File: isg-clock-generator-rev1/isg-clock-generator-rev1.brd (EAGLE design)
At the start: 76.2 x 76.2 mm, 160 parts, among them IC1 LMK03318RHSR, IC4 TPS7A8001DRBR, IC5 TPS7A8001DRBR, Q1 7M50072001, X1 OUT2_P, X2 OUT2_N, X3 OUT0_P, X4 PRIREF_P, X5 PRIREF_N, X6 V_IN_EXT

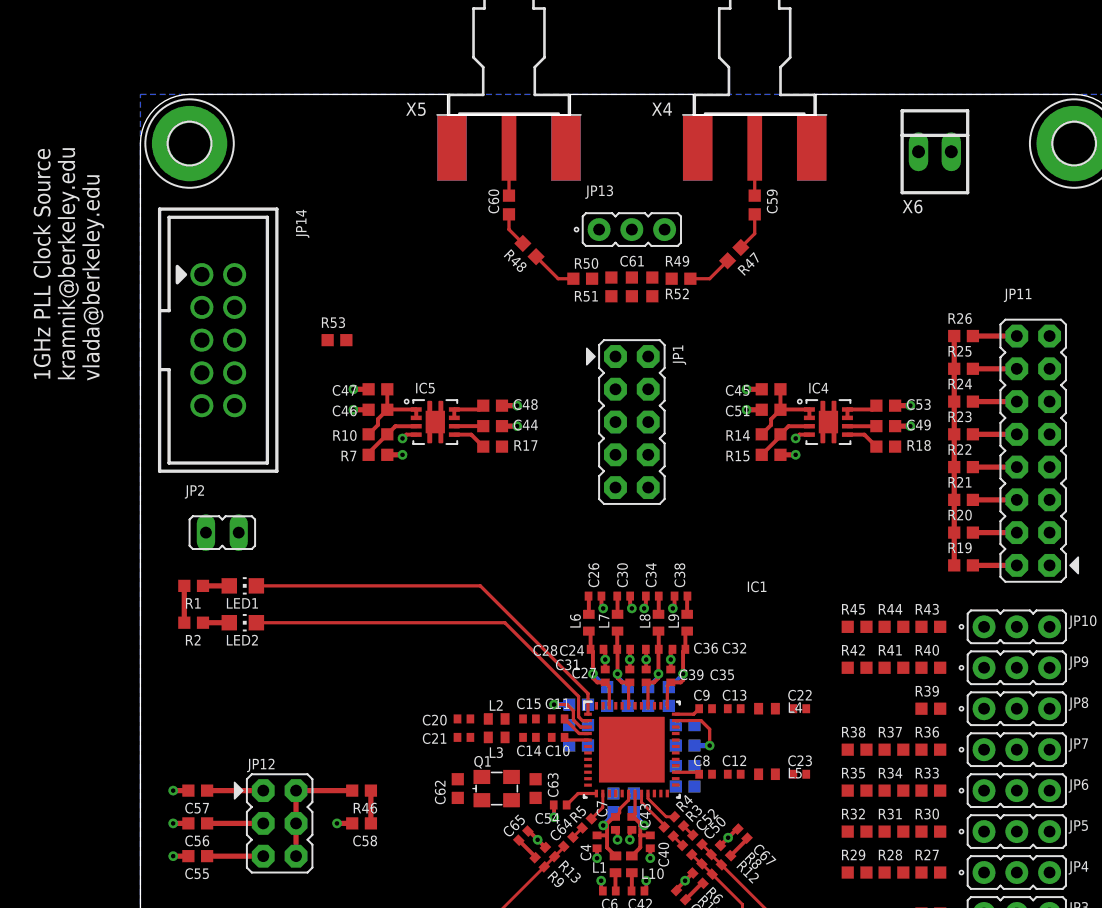
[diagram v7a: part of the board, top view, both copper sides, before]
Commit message: Crystal package fixed and routed
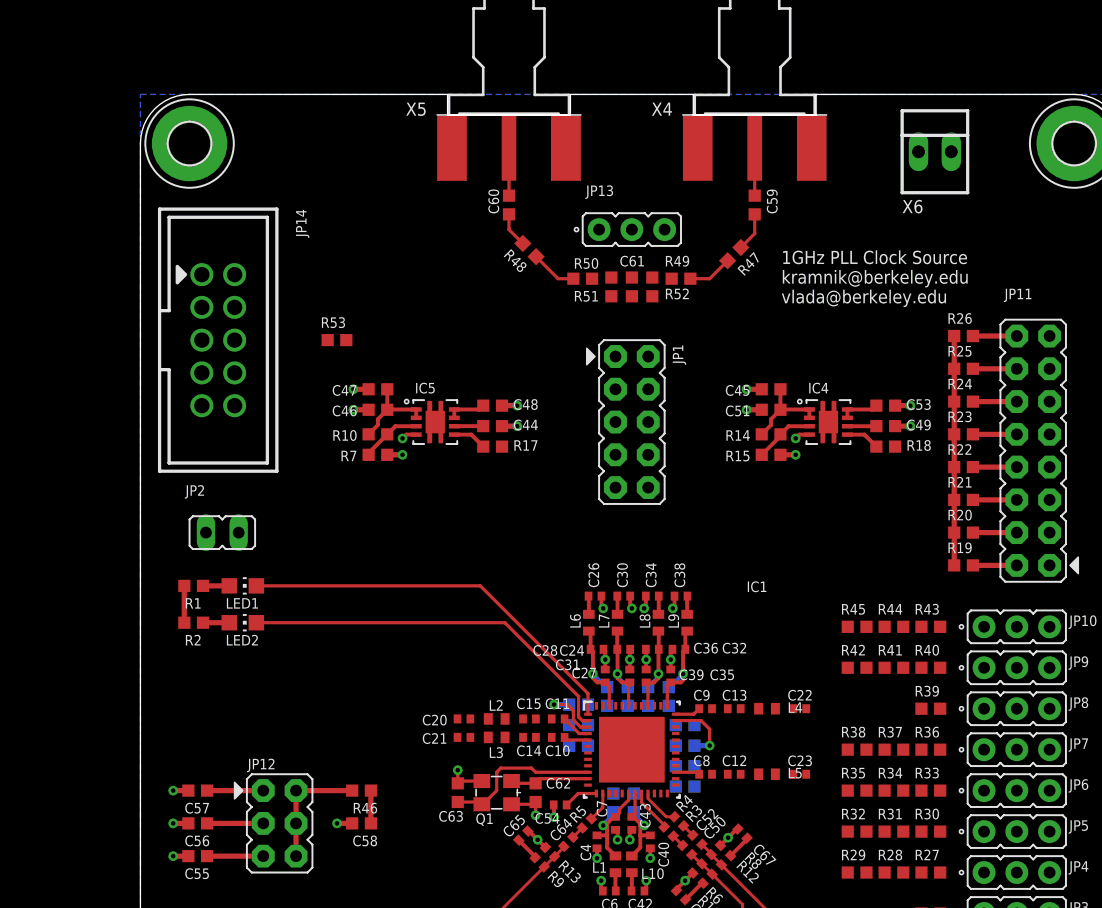
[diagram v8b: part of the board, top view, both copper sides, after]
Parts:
- Q1: device crystal-geyer_V1_0:3.2X2.5_KX-7 -> isg-clock-generator:3.2X2.5_KX-7
- moved C62 6.04 mm to (30.6, 22.1), turned to 270 degrees
- moved C63 6.04 mm to (24.6, 22.1), turned to 90 degrees
- moved Q1 0.32 mm to (27.6, 22.1), turned to 180 degrees
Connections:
- net GND: now also Q1.2, Q1.4
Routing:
- net SECREF_P: track 0.00 -> 12.3 mm
- net SECREF_N: track 0.00 -> 6.15 mm
- net GND: track 41.3 -> 47.2 mm, vias 44 -> 46
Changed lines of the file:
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@@
 <wire x1="23.8125" y1="76.2" x2="3.81" y2="76.2" width="0" layer="20"/>
 <wire x1="3.81" y1="76.2" x2="0" y2="72.39" width="0" layer="20" curve="90"/>
-<text x="-3.175" y="53.975" size="1.27" layer="21" rot="R90">1GHz PLL Clock Source
+<text x="49.68875" y="60.0075" size="1.016" layer="21">1GHz PLL Clock Source
 kramnik@berkeley.edu
 vlada@berkeley.edu</text>
@@
 <attribute name="VALUE" x="27.6225" y="1.905" size="1.016" layer="27" font="vector" ratio="16" rot="R90"/>
 </element>
-<element name="Q1" library="crystal-geyer_V1_0" library_urn="urn:adsk.eagle:library:203" package="3.2X2.5_KX-7" package3d_urn="urn:adsk.eagle:package:11924/1" value="7M50072001" x="27.6225" y="22.38375" smashed="yes">
-<attribute name="NAME" x="25.8225" y="24.08375" size="0.8128" layer="25" font="vector" ratio="16"/>
+<element name="Q1" library="isg-clock-generator" package="3.2X2.5_KX-7" package3d_urn="urn:adsk.eagle:package:11924/1" value="7M50072001" x="27.6225" y="22.06625" smashed="yes" rot="R180">
+<attribute name="NAME" x="25.98125" y="19.63875" size="0.8128" layer="25" font="vector" ratio="16"/>
 </element>
 <element name="C1" library="rcl-modified-footprints" package="C0603" package3d_urn="urn:adsk.eagle:package:23616/2" value="CAP CER 10uF 6.3V X5R 0603" x="33.9725" y="28.8925" smashed="yes" rot="MR180">
@@
 <attribute name="VALUE" x="34.544" y="67.437" size="0.8128" layer="27" font="vector" ratio="16"/>
 </element>
-<element name="C62" library="rcl-modified-footprints" package="C0603" package3d_urn="urn:adsk.eagle:package:23616/2" value="DNP" x="24.60625" y="22.38375" smashed="yes" rot="R90">
-<attribute name="NAME" x="23.65375" y="21.11375" size="0.8128" layer="25" font="vector" ratio="16" rot="R90"/>
-</element>
-<element name="C63" library="rcl-modified-footprints" package="C0603" package3d_urn="urn:adsk.eagle:package:23616/2" value="DNP" x="30.63875" y="22.38375" smashed="yes" rot="R270">
-<attribute name="NAME" x="31.59125" y="23.65375" size="0.8128" layer="25" font="vector" ratio="16" rot="R270"/>
+<element name="C62" library="rcl-modified-footprints" package="C0603" package3d_urn="urn:adsk.eagle:package:23616/2" value="DNP" x="30.63875" y="22.06625" smashed="yes" rot="R270">
+<attribute name="NAME" x="31.4325" y="22.38375" size="0.8128" layer="25" font="vector" ratio="16"/>
+</element>
+<element name="C63" library="rcl-modified-footprints" package="C0603" package3d_urn="urn:adsk.eagle:package:23616/2" value="DNP" x="24.60625" y="22.06625" smashed="yes" rot="R90">
+<attribute name="NAME" x="25.0825" y="20.6375" size="0.8128" layer="25" font="vector" ratio="16" rot="R180"/>
 </element>
 <element name="JP14" library="Kramnik's Library" package="CON_OST_302-S101" value="CON_OST_302-S101" x="6.0325" y="57.15" smashed="yes" rot="R270">
@@
 <wire x1="35.7425" y1="37.30625" x2="35.7425" y2="36.48875" width="0.3048" layer="1"/>
 <wire x1="35.7425" y1="36.48875" x2="35.8775" y2="36.35375" width="0.3048" layer="1"/>
+<contactref element="Q1" pad="4"/>
+<contactref element="Q1" pad="2"/>
+<via x="30.63875" y="20.32" extent="1-16" drill="0.35"/>
+<via x="24.60625" y="23.8125" extent="1-16" drill="0.35"/>
+<wire x1="28.7725" y1="21.16625" x2="30.46375" y2="21.16625" width="0.254" layer="1"/>
+<wire x1="30.46375" y1="21.16625" x2="30.63875" y2="21.34125" width="0.254" layer="1"/>
+<wire x1="30.63875" y1="21.34125" x2="30.63875" y2="20.32" width="0.254" layer="1"/>
+<wire x1="26.4725" y1="22.96625" x2="24.78125" y2="22.96625" width="0.254" layer="1"/>
+<wire x1="24.78125" y1="22.96625" x2="24.640625" y2="22.825625" width="0.254" layer="1"/>
+<wire x1="24.640625" y1="22.825625" x2="24.60625" y2="22.79125" width="0.254" layer="1"/>
+<wire x1="24.60625" y1="23.8125" x2="24.60625" y2="22.86" width="0.254" layer="1"/>
+<wire x1="24.60625" y1="22.86" x2="24.640625" y2="22.825625" width="0.254" layer="1"/>
 <wire x1="52.0446" y1="72.0471" x2="52.0446" y2="72.0471" width="0" layer="19" extent="1-16"/>
 <wire x1="43.2054" y1="72.0471" x2="43.2054" y2="72.0471" width="0" layer="19" extent="1-16"/>
@@
 <wire x1="33.6804" y1="4.1529" x2="33.6804" y2="4.1529" width="0" layer="19" extent="1-16"/>
 <wire x1="23.4696" y1="4.1529" x2="23.4696" y2="4.1529" width="0" layer="19" extent="1-16"/>
-<wire x1="30.63875" y1="21.65875" x2="32.04375" y2="21.11375" width="0" layer="19" extent="1-1"/>
 <wire x1="53.34" y1="50.8" x2="51.865" y2="49.825" width="0" layer="19" extent="1-1"/>
 <wire x1="22.86" y1="50.8" x2="21.385" y2="49.825" width="0" layer="19" extent="1-1"/>
+<wire x1="24.5825" y1="26.3525" x2="24.60625" y2="23.8125" width="0" layer="19" extent="1-1"/>
+<wire x1="24.5825" y1="27.78125" x2="24.5825" y2="26.3525" width="0" layer="19" extent="1-1"/>
 <wire x1="31.885" y1="27.78125" x2="34.6975" y2="27.305" width="0" layer="19" extent="1-16"/>
 <wire x1="31.885" y1="26.3525" x2="31.885" y2="27.78125" width="0" layer="19" extent="1-1"/>
@@
 <wire x1="54.8375" y1="15.875" x2="54.8375" y2="19.05" width="0" layer="19" extent="1-1"/>
 <wire x1="51.6175" y1="23.495" x2="54.8375" y2="22.225" width="0" layer="19" extent="1-1"/>
-<wire x1="24.5825" y1="26.3525" x2="29.6625" y2="26.3525" width="0" layer="19" extent="1-1"/>
-<wire x1="24.5825" y1="27.78125" x2="24.5825" y2="26.3525" width="0" layer="19" extent="1-1"/>
-<wire x1="24.60625" y1="23.10875" x2="24.5825" y2="26.3525" width="0" layer="19" extent="1-1"/>
 <wire x1="38.1" y1="60.5525" x2="35.56" y2="65.7225" width="0" layer="19" extent="1-1"/>
 <wire x1="39.6875" y1="60.5525" x2="38.1" y2="60.5525" width="0" layer="19" extent="1-1"/>
@@
 <contactref element="Q1" pad="3"/>
 <contactref element="C63" pad="1"/>
-<wire x1="30.63875" y1="23.10875" x2="34.700003125" y2="23.65" width="0" layer="19" extent="1-1"/>
-<wire x1="28.7725" y1="23.28375" x2="30.63875" y2="23.10875" width="0" layer="19" extent="1-1"/>
+<wire x1="24.60625" y1="21.34125" x2="26.2975" y2="21.34125" width="0.254" layer="1"/>
+<wire x1="26.2975" y1="21.34125" x2="26.4725" y2="21.16625" width="0.254" layer="1"/>
+<wire x1="34.700003125" y1="23.65" x2="30.6425" y2="23.65" width="0.254" layer="1"/>
+<wire x1="30.6425" y1="23.65" x2="30.32125" y2="23.97125" width="0.254" layer="1"/>
+<wire x1="30.32125" y1="23.97125" x2="27.94" y2="23.97125" width="0.254" layer="1"/>
+<wire x1="27.94" y1="23.97125" x2="27.6225" y2="23.65375" width="0.254" layer="1"/>
+<wire x1="27.6225" y1="23.65375" x2="27.6225" y2="22.225" width="0.254" layer="1"/>
+<wire x1="26.56375" y1="21.16625" x2="26.4725" y2="21.16625" width="0.254" layer="1"/>
+<wire x1="27.6225" y1="22.225" x2="26.56375" y2="21.16625" width="0.254" layer="1"/>
 </signal>
 <signal name="PRIREF_N">
@@
 <contactref element="Q1" pad="1"/>
 <contactref element="IC1" pad="11"/>
-<wire x1="26.4725" y1="21.48375" x2="34.700003125" y2="23.150003125" width="0" layer="19" extent="1-1"/>
-<wire x1="24.60625" y1="21.65875" x2="26.4725" y2="21.48375" width="0" layer="19" extent="1-1"/>
+<wire x1="30.63875" y1="22.79125" x2="28.9475" y2="22.79125" width="0.254" layer="1"/>
+<wire x1="28.9475" y1="22.79125" x2="28.7725" y2="22.96625" width="0.254" layer="1"/>
+<wire x1="34.700003125" y1="23.150003125" x2="30.997503125" y2="23.150003125" width="0.254" layer="1"/>
+<wire x1="30.997503125" y1="23.150003125" x2="30.63875" y2="22.79125" width="0.254" layer="1"/>
 </signal>
 <signal name="N$5">
